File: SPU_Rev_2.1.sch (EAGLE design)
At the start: 258 parts, among them Q1 12MHz

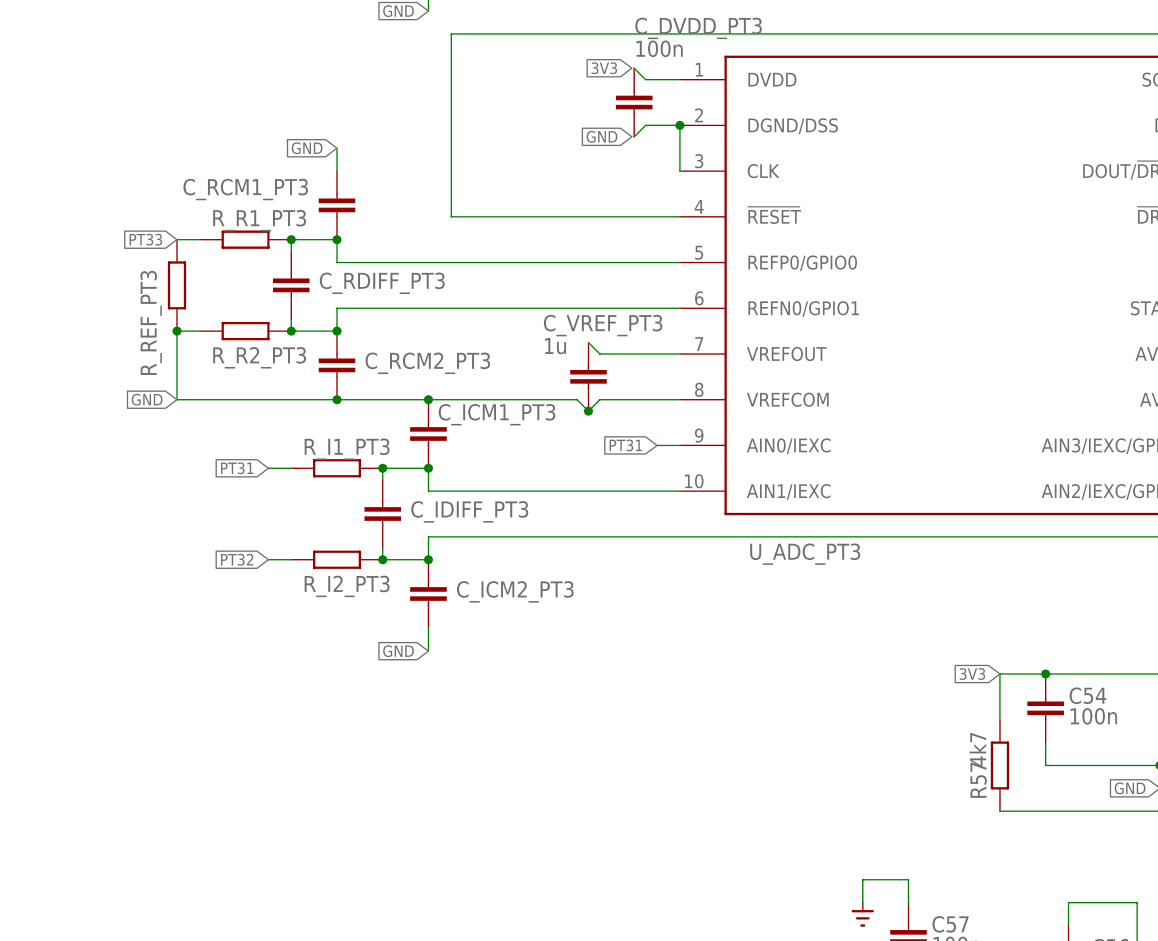
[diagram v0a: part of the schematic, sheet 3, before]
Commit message: Added PT100 ADC R/C values
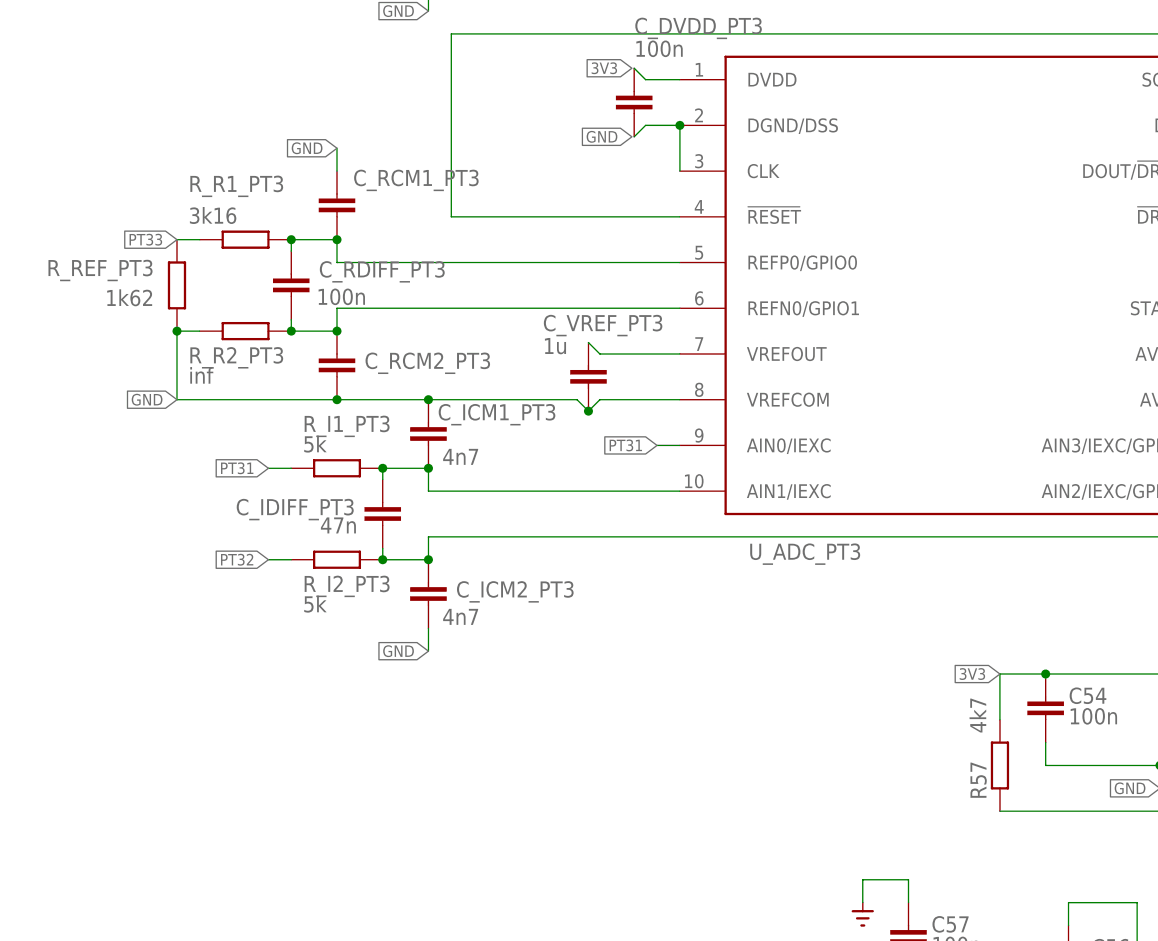
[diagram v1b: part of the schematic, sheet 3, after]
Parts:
- C_ICM1_PT3, C_ICM2_PT3: value (none) -> 4n7
- C_IDIFF_PT3: value (none) -> 47n
- C_RDIFF_PT3: value (none) -> 100n
- R_I1_PT3, R_I2_PT3: value (none) -> 5k
- R_R1_PT3: value (none) -> 3k16
- R_R2_PT3: value (none) -> inf
- R_REF_PT3: value (none) -> 1k62
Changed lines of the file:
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@@
 <part name="RN_B_PT2" library="resistor-dil" library_urn="urn:adsk.eagle:library:342" deviceset="4R-N" device="0603-ARC" package3d_urn="urn:adsk.eagle:package:24926/1" value="47"/>
 <part name="U_ADC_PT3" library="ads11xx" deviceset="ADS1147" device="TSSOP20" package3d_urn="urn:adsk.eagle:package:4349/2"/>
-<part name="R_REF_PT3" library="++Bedrahtet" deviceset="R-EU_" device="R0603"/>
-<part name="R_R1_PT3" library="++Bedrahtet" deviceset="R-EU_" device="R0603"/>
-<part name="R_R2_PT3" library="++Bedrahtet" deviceset="R-EU_" device="R0603"/>
-<part name="C_RDIFF_PT3" library="rcl" library_urn="urn:adsk.eagle:library:334" deviceset="C-EU" device="C0603" package3d_urn="urn:adsk.eagle:package:23616/2"/>
+<part name="R_REF_PT3" library="++Bedrahtet" deviceset="R-EU_" device="R0603" value="1k62"/>
+<part name="R_R1_PT3" library="++Bedrahtet" deviceset="R-EU_" device="R0603" value="3k16"/>
+<part name="R_R2_PT3" library="++Bedrahtet" deviceset="R-EU_" device="R0603" value="inf"/>
+<part name="C_RDIFF_PT3" library="rcl" library_urn="urn:adsk.eagle:library:334" deviceset="C-EU" device="C0603" package3d_urn="urn:adsk.eagle:package:23616/2" value="100n"/>
 <part name="C_RCM1_PT3" library="rcl" library_urn="urn:adsk.eagle:library:334" deviceset="C-EU" device="C0603" package3d_urn="urn:adsk.eagle:package:23616/2"/>
 <part name="C_RCM2_PT3" library="rcl" library_urn="urn:adsk.eagle:library:334" deviceset="C-EU" device="C0603" package3d_urn="urn:adsk.eagle:package:23616/2"/>
-<part name="R_I1_PT3" library="++Bedrahtet" deviceset="R-EU_" device="R0603"/>
-<part name="R_I2_PT3" library="++Bedrahtet" deviceset="R-EU_" device="R0603"/>
-<part name="C_IDIFF_PT3" library="rcl" library_urn="urn:adsk.eagle:library:334" deviceset="C-EU" device="C0603" package3d_urn="urn:adsk.eagle:package:23616/2"/>
-<part name="C_ICM1_PT3" library="rcl" library_urn="urn:adsk.eagle:library:334" deviceset="C-EU" device="C0603" package3d_urn="urn:adsk.eagle:package:23616/2"/>
-<part name="C_ICM2_PT3" library="rcl" library_urn="urn:adsk.eagle:library:334" deviceset="C-EU" device="C0603" package3d_urn="urn:adsk.eagle:package:23616/2"/>
+<part name="R_I1_PT3" library="++Bedrahtet" deviceset="R-EU_" device="R0603" value="5k"/>
+<part name="R_I2_PT3" library="++Bedrahtet" deviceset="R-EU_" device="R0603" value="5k"/>
+<part name="C_IDIFF_PT3" library="rcl" library_urn="urn:adsk.eagle:library:334" deviceset="C-EU" device="C0603" package3d_urn="urn:adsk.eagle:package:23616/2" value="47n"/>
+<part name="C_ICM1_PT3" library="rcl" library_urn="urn:adsk.eagle:library:334" deviceset="C-EU" device="C0603" package3d_urn="urn:adsk.eagle:package:23616/2" value="4n7"/>
+<part name="C_ICM2_PT3" library="rcl" library_urn="urn:adsk.eagle:library:334" deviceset="C-EU" device="C0603" package3d_urn="urn:adsk.eagle:package:23616/2" value="4n7"/>
 <part name="C_VREF_PT3" library="rcl" library_urn="urn:adsk.eagle:library:334" deviceset="C-EU" device="C0603" package3d_urn="urn:adsk.eagle:package:23616/2" value="1u"/>
 <part name="C_DVDD_PT3" library="rcl" library_urn="urn:adsk.eagle:library:334" deviceset="C-EU" device="C0603" package3d_urn="urn:adsk.eagle:package:23616/2" value="100n"/>
@@
 </instance>
 <instance part="R_REF_PT3" gate="G$1" x="22.86" y="-271.78" smashed="yes" rot="R90">
-<attribute name="NAME" x="20.5994" y="-281.94" size="1.778" layer="95" rot="R90"/>
-<attribute name="VALUE" x="26.162" y="-275.59" size="1.778" layer="96" rot="R90"/>
+<attribute name="NAME" x="20.32" y="-268.9606" size="1.778" layer="95" rot="R180"/>
+<attribute name="VALUE" x="20.32" y="-272.288" size="1.778" layer="96" rot="R180"/>
 </instance>
 <instance part="R_R1_PT3" gate="G$1" x="30.48" y="-266.7" smashed="yes" rot="R180">
-<attribute name="NAME" x="26.67" y="-265.2014" size="1.778" layer="95"/>
-<attribute name="VALUE" x="34.29" y="-263.398" size="1.778" layer="96" rot="R180"/>
+<attribute name="NAME" x="24.13" y="-261.3914" size="1.778" layer="95"/>
+<attribute name="VALUE" x="24.13" y="-264.922" size="1.778" layer="96"/>
 </instance>
 <instance part="R_R2_PT3" gate="G$1" x="30.48" y="-276.86" smashed="yes" rot="R180">
-<attribute name="NAME" x="26.67" y="-280.4414" size="1.778" layer="95"/>
-<attribute name="VALUE" x="34.29" y="-273.558" size="1.778" layer="96" rot="R180"/>
+<attribute name="NAME" x="24.13" y="-280.4414" size="1.778" layer="95"/>
+<attribute name="VALUE" x="24.13" y="-282.702" size="1.778" layer="96"/>
 </instance>
 <instance part="C_RDIFF_PT3" gate="G$1" x="35.56" y="-270.51" smashed="yes">
-<attribute name="NAME" x="38.608" y="-272.161" size="1.778" layer="95"/>
-<attribute name="VALUE" x="37.084" y="-275.209" size="1.778" layer="96"/>
+<attribute name="NAME" x="38.608" y="-270.891" size="1.778" layer="95"/>
+<attribute name="VALUE" x="38.354" y="-273.939" size="1.778" layer="96"/>
 </instance>
 <instance part="C_RCM1_PT3" gate="G$1" x="40.64" y="-261.62" smashed="yes">
-<attribute name="NAME" x="37.592" y="-259.969" size="1.778" layer="95" rot="R180"/>
+<attribute name="NAME" x="42.418" y="-260.731" size="1.778" layer="95"/>
 <attribute name="VALUE" x="42.164" y="-266.319" size="1.778" layer="96"/>
 </instance>
@@
 </instance>
 <instance part="R_I1_PT3" gate="G$1" x="40.64" y="-292.1" smashed="yes" rot="R180">
-<attribute name="NAME" x="36.83" y="-290.6014" size="1.778" layer="95"/>
-<attribute name="VALUE" x="44.45" y="-288.798" size="1.778" layer="96" rot="R180"/>
+<attribute name="NAME" x="36.83" y="-288.0614" size="1.778" layer="95"/>
+<attribute name="VALUE" x="36.83" y="-290.322" size="1.778" layer="96"/>
 </instance>
 <instance part="R_I2_PT3" gate="G$1" x="40.64" y="-302.26" smashed="yes" rot="R180">
 <attribute name="NAME" x="36.83" y="-305.8414" size="1.778" layer="95"/>
-<attribute name="VALUE" x="44.45" y="-298.958" size="1.778" layer="96" rot="R180"/>
+<attribute name="VALUE" x="36.83" y="-308.102" size="1.778" layer="96"/>
 </instance>
 <instance part="C_IDIFF_PT3" gate="G$1" x="45.72" y="-295.91" smashed="yes">
-<attribute name="NAME" x="48.768" y="-297.561" size="1.778" layer="95"/>
-<attribute name="VALUE" x="47.244" y="-300.609" size="1.778" layer="96"/>
+<attribute name="NAME" x="42.672" y="-295.529" size="1.778" layer="95" rot="R180"/>
+<attribute name="VALUE" x="42.926" y="-297.561" size="1.778" layer="96" rot="R180"/>
 </instance>
 <instance part="C_ICM1_PT3" gate="G$1" x="50.8" y="-287.02" smashed="yes">
@@
 <instance part="R57" gate="G$1" x="114.3" y="-325.12" smashed="yes" rot="R270">
 <attribute name="NAME" x="112.8014" y="-328.93" size="1.778" layer="95" rot="R90"/>
-<attribute name="VALUE" x="110.998" y="-321.31" size="1.778" layer="96" rot="R270"/>
+<attribute name="VALUE" x="110.998" y="-317.5" size="1.778" layer="96" rot="R270"/>
 </instance>
 <instance part="R58" gate="G$1" x="205.74" y="-340.36" smashed="yes">

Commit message: RS422 confirmed
RS422 driver functionality plus optocouplers tested and confirmed
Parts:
- JP_MS, X_PROG: value (none) -> x
- LED7, LED8: value (none) -> 1V9
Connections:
- net PRD_ON renamed PDR_ON
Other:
- note added: "functionality confirmed"
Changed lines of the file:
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@@
 <part name="R18" library="rcl" library_urn="urn:adsk.eagle:library:334" deviceset="R-EU_" device="R0805" package3d_urn="urn:adsk.eagle:package:23553/2" value="680"/>
 <part name="R19" library="rcl" library_urn="urn:adsk.eagle:library:334" deviceset="R-EU_" device="R0805" package3d_urn="urn:adsk.eagle:package:23553/2" value="330"/>
-<part name="LED7" library="adafruit" library_urn="urn:adsk.eagle:library:420" deviceset="LED" device="CHIP-LED0805" package3d_urn="urn:adsk.eagle:package:6240557/1"/>
+<part name="LED7" library="adafruit" library_urn="urn:adsk.eagle:library:420" deviceset="LED" device="CHIP-LED0805" package3d_urn="urn:adsk.eagle:package:6240557/1" value="1V9"/>
 <part name="R20" library="rcl" library_urn="urn:adsk.eagle:library:334" deviceset="R-EU_" device="R0805" package3d_urn="urn:adsk.eagle:package:23553/2" value="4k7"/>
-<part name="LED8" library="adafruit" library_urn="urn:adsk.eagle:library:420" deviceset="LED" device="CHIP-LED0805" package3d_urn="urn:adsk.eagle:package:6240557/1"/>
+<part name="LED8" library="adafruit" library_urn="urn:adsk.eagle:library:420" deviceset="LED" device="CHIP-LED0805" package3d_urn="urn:adsk.eagle:package:6240557/1" value="1V9"/>
 <part name="R21" library="rcl" library_urn="urn:adsk.eagle:library:334" deviceset="R-EU_" device="R0805" package3d_urn="urn:adsk.eagle:package:23553/2" value="470"/>
 <part name="U_ADR366_3" library="ADR360" deviceset="ADR36*" device="UJZ" technology="_" value="ADR366WAUJZ"/>
@@
 <part name="R28" library="rcl" library_urn="urn:adsk.eagle:library:334" deviceset="R-EU_" device="R0805" package3d_urn="urn:adsk.eagle:package:23553/2" value="99M"/>
 <part name="R29" library="rcl" library_urn="urn:adsk.eagle:library:334" deviceset="R-EU_" device="R0805" package3d_urn="urn:adsk.eagle:package:23553/2" value="10k"/>
-<part name="JP_MS" library="aSparkFun" deviceset="M02" device="PTH"/>
+<part name="JP_MS" library="aSparkFun" deviceset="M02" device="PTH" value="x"/>
 <part name="D11" library="diodes" deviceset="DZ" device="MELF" value="3V6"/>
 <part name="D12" library="diodes" deviceset="DZ" device="MELF" value="3V6"/>
@@
 <part name="X_MIRROR" library="con-ept-One27" deviceset="403-5X026-5X" device=""/>
 <part name="X_MIRROR1" library="con-ept-One27" deviceset="403-5X026-5X" device=""/>
-<part name="X_PROG" library="con-lstb" library_urn="urn:adsk.eagle:library:162" deviceset="MA10-2" device="" package3d_urn="urn:adsk.eagle:package:8331/1"/>
+<part name="X_PROG" library="con-lstb" library_urn="urn:adsk.eagle:library:162" deviceset="MA10-2" device="" package3d_urn="urn:adsk.eagle:package:8331/1" value="x"/>
 <part name="X_RXSM-DAPI" library="con-ept-One27" deviceset="403-5X020-5X" device=""/>
 <part name="U_ADC_DMS1" library="ads11xx" deviceset="ADS1147" device="TSSOP20" package3d_urn="urn:adsk.eagle:package:4349/2"/>
@@
 </segment>
 </net>
-<net name="PRD_ON" class="0">
+<net name="PDR_ON" class="0">
 <segment>
 <pinref part="U_STM32F779" gate="G$1" pin="PDR_ON"/>
@@
 <wire x1="139.446" y1="213.868" x2="134.366" y2="213.868" width="0.1524" layer="94"/>
 <text x="49.784" y="137.16" size="1.27" layer="94">LM78L05ACMX/NOPB</text>
-<wire x1="127.508" y1="191.262" x2="157.734" y2="191.516" width="0.1524" layer="94" style="shortdash"/>
-<wire x1="157.734" y1="191.516" x2="157.48" y2="169.418" width="0.1524" layer="94" style="shortdash"/>
-<wire x1="157.48" y1="169.418" x2="127.254" y2="169.164" width="0.1524" layer="94" style="shortdash"/>
-<wire x1="127.254" y1="169.164" x2="127.508" y2="191.262" width="0.1524" layer="94" style="shortdash"/>
-<wire x1="181.356" y1="143.002" x2="181.61" y2="168.91" width="0.1524" layer="94" style="shortdash"/>
-<wire x1="181.61" y1="168.91" x2="157.988" y2="168.91" width="0.1524" layer="94" style="shortdash"/>
-<wire x1="181.356" y1="143.002" x2="157.734" y2="143.002" width="0.1524" layer="94" style="shortdash"/>
-<wire x1="157.734" y1="143.002" x2="157.988" y2="168.91" width="0.1524" layer="94" style="shortdash"/>
+<wire x1="127" y1="191.77" x2="157.48" y2="191.77" width="0.1524" layer="94" style="shortdash"/>
+<wire x1="157.48" y1="191.77" x2="157.48" y2="168.91" width="0.1524" layer="94" style="shortdash"/>
+<wire x1="157.48" y1="168.91" x2="127" y2="168.91" width="0.1524" layer="94" style="shortdash"/>
+<wire x1="127" y1="168.91" x2="127" y2="191.77" width="0.1524" layer="94" style="shortdash"/>
+<wire x1="181.61" y1="143.51" x2="181.61" y2="168.91" width="0.1524" layer="94" style="shortdash"/>
+<wire x1="181.61" y1="168.91" x2="158.75" y2="168.91" width="0.1524" layer="94" style="shortdash"/>
+<wire x1="181.61" y1="143.51" x2="158.75" y2="143.51" width="0.1524" layer="94" style="shortdash"/>
+<wire x1="158.75" y1="143.51" x2="158.75" y2="168.91" width="0.1524" layer="94" style="shortdash"/>
 <text x="208.026" y="213.106" size="5.08" layer="94">RS422 driver</text>
 <text x="180.34" y="291.592" size="7.62" layer="94">logic side    &lt;-&gt;  RXSM side</text>
@@
 <text x="40.64" y="-370.84" size="1.27" layer="97">WE-SL3 SMT COMMON
 MODE LINE FILT</text>
+<wire x1="96.52" y1="137.16" x2="190.5" y2="137.16" width="0.4572" layer="88"/>
+<wire x1="190.5" y1="137.16" x2="190.5" y2="60.96" width="0.4572" layer="88"/>
+<wire x1="190.5" y1="60.96" x2="96.52" y2="60.96" width="0.4572" layer="88"/>
+<wire x1="96.52" y1="60.96" x2="96.52" y2="137.16" width="0.4572" layer="88"/>
+<wire x1="87.63" y1="143.51" x2="87.63" y2="96.52" width="0.4572" layer="88"/>
+<wire x1="87.63" y1="96.52" x2="31.75" y2="96.52" width="0.4572" layer="88"/>
+<wire x1="31.75" y1="96.52" x2="31.75" y2="143.51" width="0.4572" layer="88"/>
+<wire x1="31.75" y1="143.51" x2="87.63" y2="143.51" width="0.4572" layer="88"/>
+<wire x1="24.13" y1="181.61" x2="97.79" y2="181.61" width="0.4572" layer="88"/>
+<wire x1="97.79" y1="181.61" x2="97.79" y2="147.32" width="0.4572" layer="88"/>
+<wire x1="97.79" y1="147.32" x2="24.13" y2="147.32" width="0.4572" layer="88"/>
+<wire x1="24.13" y1="147.32" x2="24.13" y2="181.61" width="0.4572" layer="88"/>
+<wire x1="382.27" y1="288.29" x2="466.09" y2="288.29" width="0.4572" layer="88"/>
+<wire x1="466.09" y1="288.29" x2="466.09" y2="298.45" width="0.4572" layer="88"/>
+<wire x1="466.09" y1="298.45" x2="382.27" y2="298.45" width="0.4572" layer="88"/>
+<wire x1="382.27" y1="298.45" x2="382.27" y2="288.29" width="0.4572" layer="88"/>
+<text x="387.35" y="290.83" size="5.08" layer="88">functionality confirmed</text>
+<wire x1="123.19" y1="193.04" x2="184.15" y2="193.04" width="0.4572" layer="88"/>
+<wire x1="184.15" y1="193.04" x2="184.15" y2="139.7" width="0.4572" layer="88"/>
+<wire x1="184.15" y1="139.7" x2="123.19" y2="139.7" width="0.4572" layer="88"/>
+<wire x1="123.19" y1="139.7" x2="123.19" y2="193.04" width="0.4572" layer="88"/>
+<wire x1="200.66" y1="212.09" x2="273.05" y2="212.09" width="0.4572" layer="88"/>
+<wire x1="273.05" y1="212.09" x2="273.05" y2="154.94" width="0.4572" layer="88"/>
+<wire x1="273.05" y1="154.94" x2="200.66" y2="154.94" width="0.4572" layer="88"/>
+<wire x1="200.66" y1="154.94" x2="200.66" y2="212.09" width="0.4572" layer="88"/>
 </plain>
 <instances>
